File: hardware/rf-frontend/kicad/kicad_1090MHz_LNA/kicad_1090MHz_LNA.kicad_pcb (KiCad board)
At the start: 2 copper layers, 27.8 x 18.5 mm, 11 parts, among them IC1 PGA-103_, X1 STA1090EC

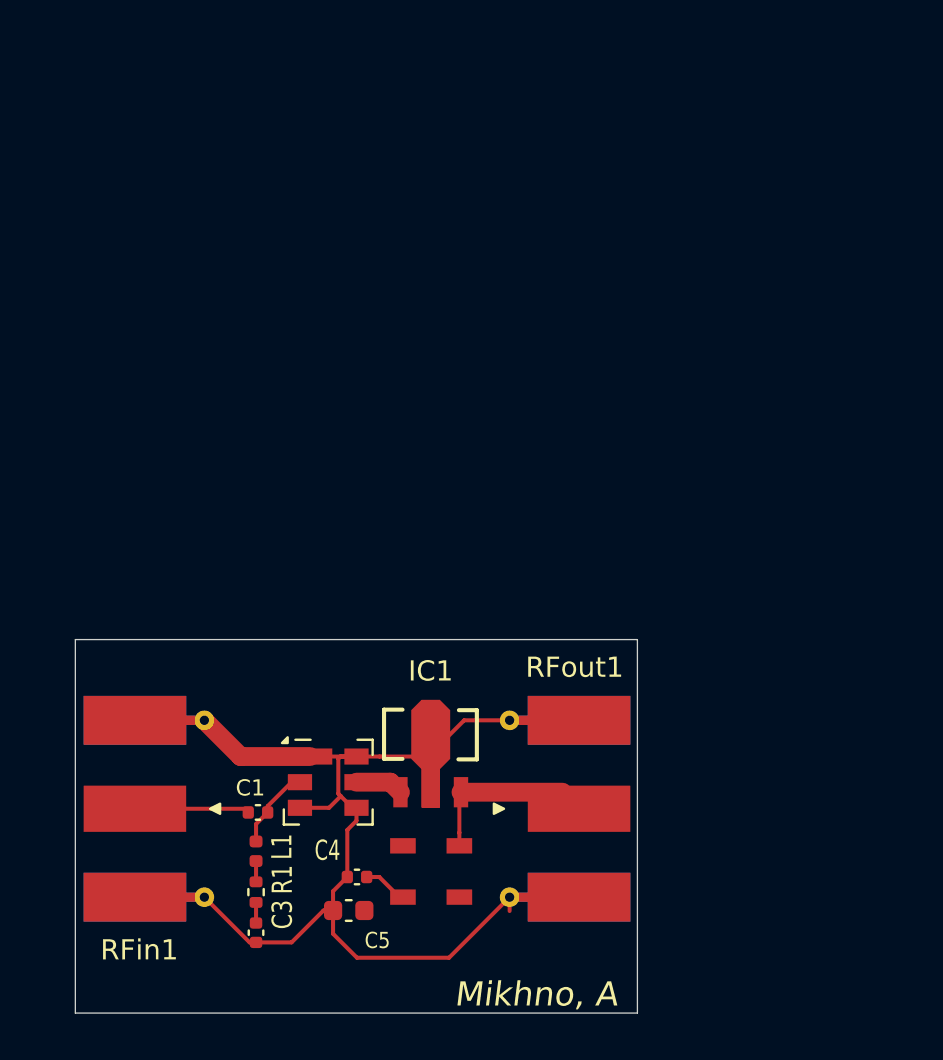
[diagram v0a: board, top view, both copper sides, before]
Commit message: Update RF frontend KiCad: completed USB-C LNA board with routing, pours, via stitching, and Gerbers
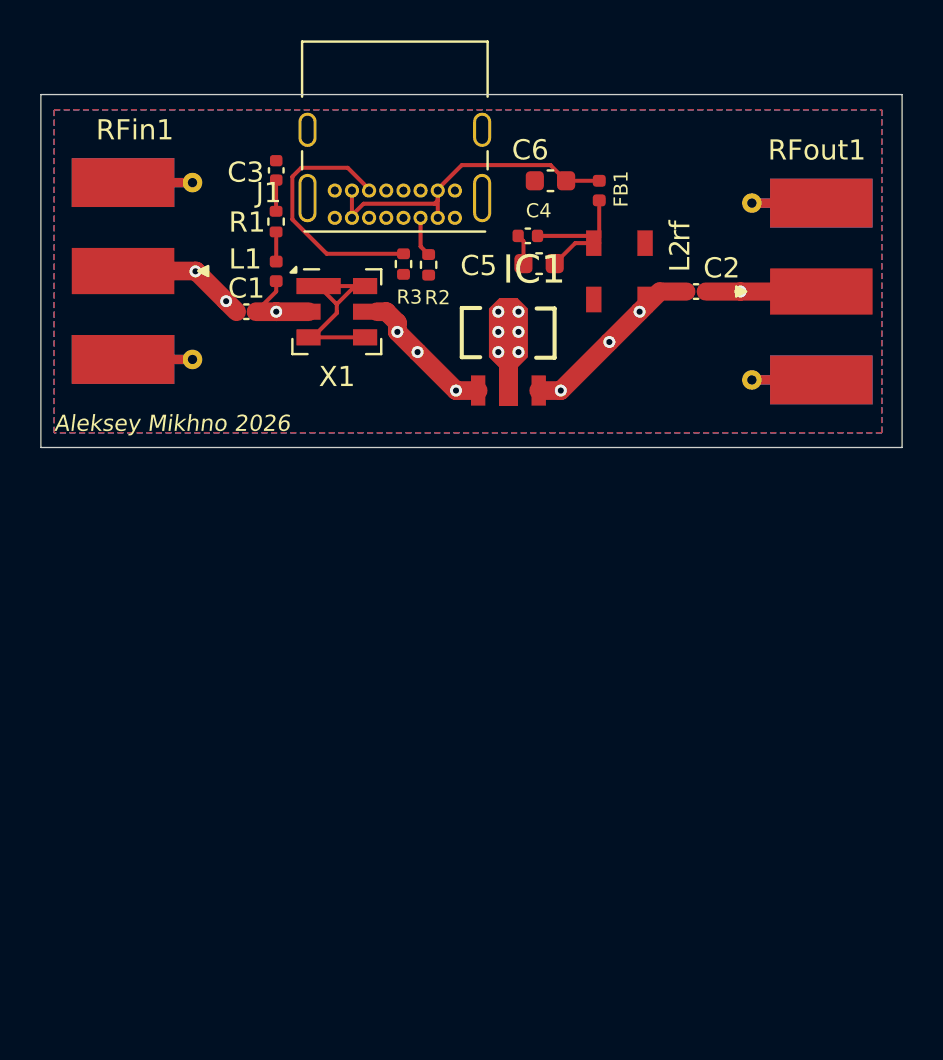
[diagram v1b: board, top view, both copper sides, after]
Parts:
- added C2: C, Capacitor_SMD:C_0402_1005Metric, F.Cu at (163.8, 77.0)
- added C6: C, Capacitor_SMD:C_0603_1608Metric, F.Cu at (156.6, 71.5)
- added FB1: FerriteBead, Inductor_SMD:L_0402_1005Metric, F.Cu at (159.0, 72.0)
- added J1: USB_C_Receptacle_USB2.0_16P, Connector_USB:USB_C_Receptacle_GCT_USB4085, F.Cu at (151.8, 73.3)
- added R2: R, Resistor_SMD:R_0402_1005Metric, F.Cu at (150.5, 75.7)
- added R3: R, Resistor_SMD:R_0402_1005Metric, F.Cu at (149.3, 75.6)
- C1: value 0.01uF -> C
- C3: value 330pF -> C
- C4: value 0.33uF -> C
- C5: value 10uF -> C
- L1: value 620nH -> L
- R1: value 150Ω -> R
- moved C3 37.8 mm to (143.0, 71.0), turned to -90 degrees
- moved C5 33.4 mm to (156.0, 75.6)
- moved R1 33.2 mm to (143.0, 73.5), turned to 90 degrees
- moved C4 32.9 mm to (155.5, 74.2)
- moved L2 31.2 mm to (160.0, 76.0), turned to 180 degrees
- moved L1 28.7 mm to (143.0, 76.0), turned to 90 degrees
- moved RFout1 28.3 mm to (168.3, 77.0)
- moved RFin1 26.6 mm to (137.1, 76.0)
- moved C1 24.8 mm to (141.5, 78.0)
- moved X1 23.3 mm to (146.0, 78.0)
- moved IC1 20.3 mm to (154.4, 78.9)
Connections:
- RFout1 pad 1: Net-(IC1-OUT/DC) -> Net-(C2-Pad2)
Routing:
- net GND: track 49.0 -> 12.0 mm, vias 0 -> 6
- net Net-(C6-Pad1): track 0.00 -> 16.8 mm
- net Net-(J1-CC2): track 0.00 -> 12.8 mm
- net Net-(L2-DC): track 2.29 -> 8.06 mm
- net Net-(C2-Pad2): track 0.00 -> 5.72 mm, vias 0 -> 1
- net Net-(IC1-IN): track 2.38 -> 7.49 mm, vias 0 -> 3
- net Net-(J1-CC1): track 0.00 -> 1.98 mm
- net Net-(C1-Pad1): track 5.69 -> 6.46 mm, vias 0 -> 2
- net Net-(C3-Pad2): track 1.02 -> 1.55 mm
- net Net-(IC1-OUT/DC): track 8.89 -> 9.35 mm, vias 0 -> 3
- net Net-(X1-IN): track 4.08 -> 4.53 mm, vias 0 -> 1
- added copper zone on B.Cu, net GND
- added copper zone on F.Cu, net GND
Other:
- board size 27.8 x 18.5 mm -> 42.7 x 17.5 mm
- board text added: "Aleksey Mikhno 2026"
- board text removed: "Mikhno, A"
